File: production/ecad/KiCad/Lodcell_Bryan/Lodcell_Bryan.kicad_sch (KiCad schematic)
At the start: 24 parts, among them J1 LoadCellConnector, J2 power_for_Loadcell, J3 ConnToESP32, U3 ADS1231IDR, U4 TXB0104DR

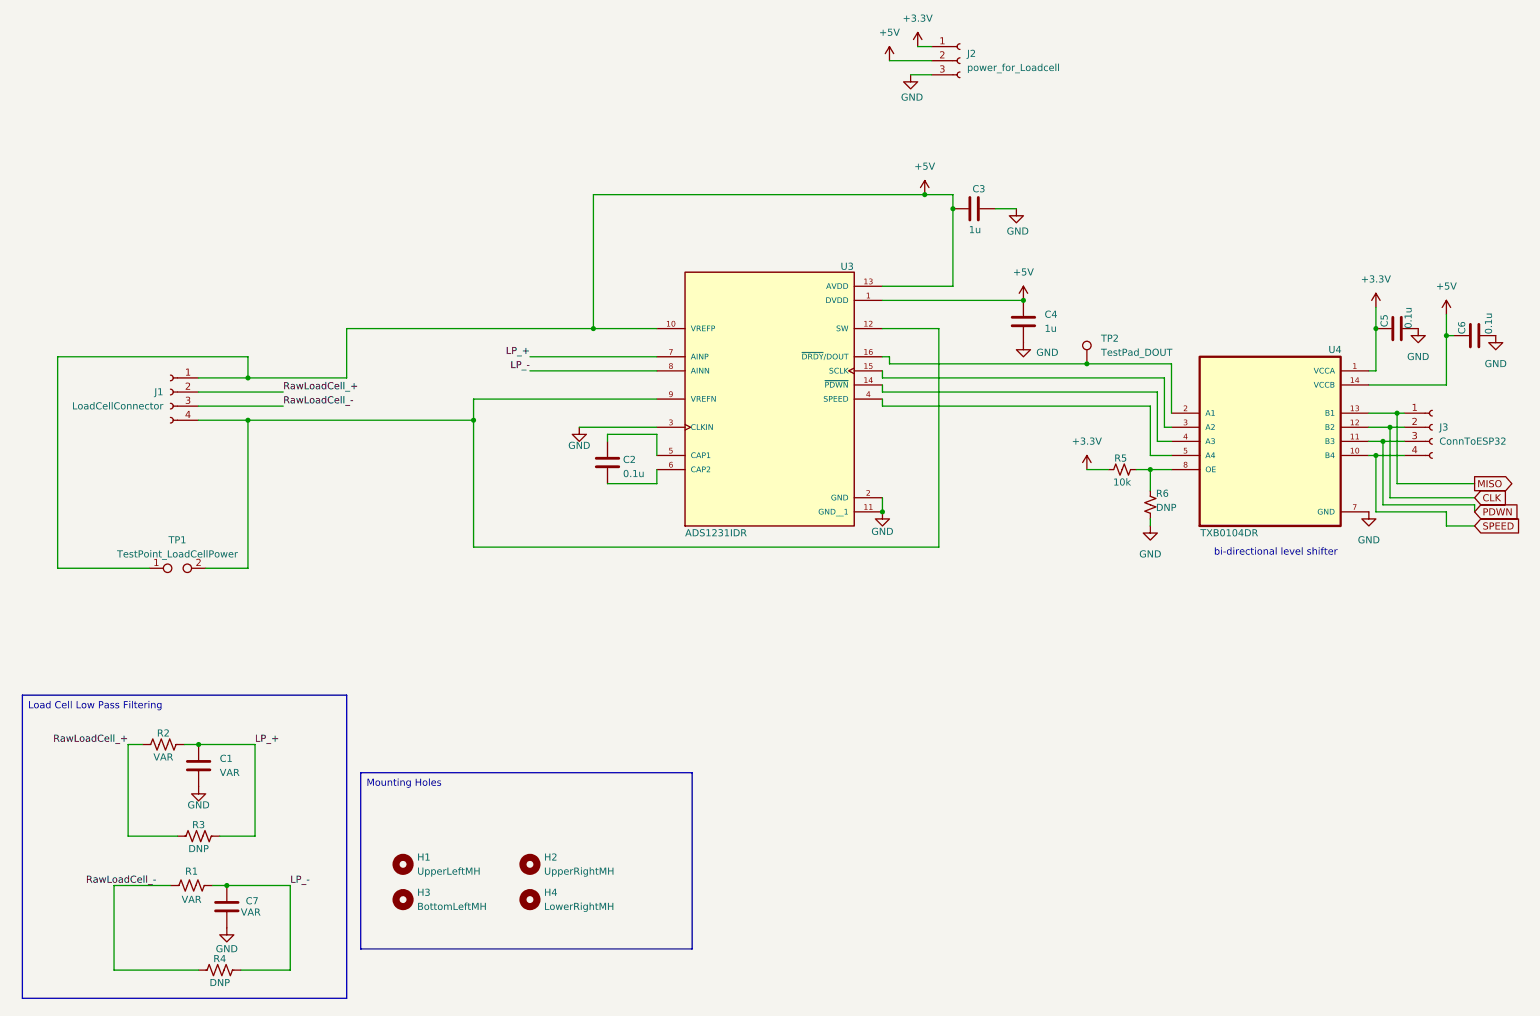
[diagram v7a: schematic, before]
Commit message: Renamed designators
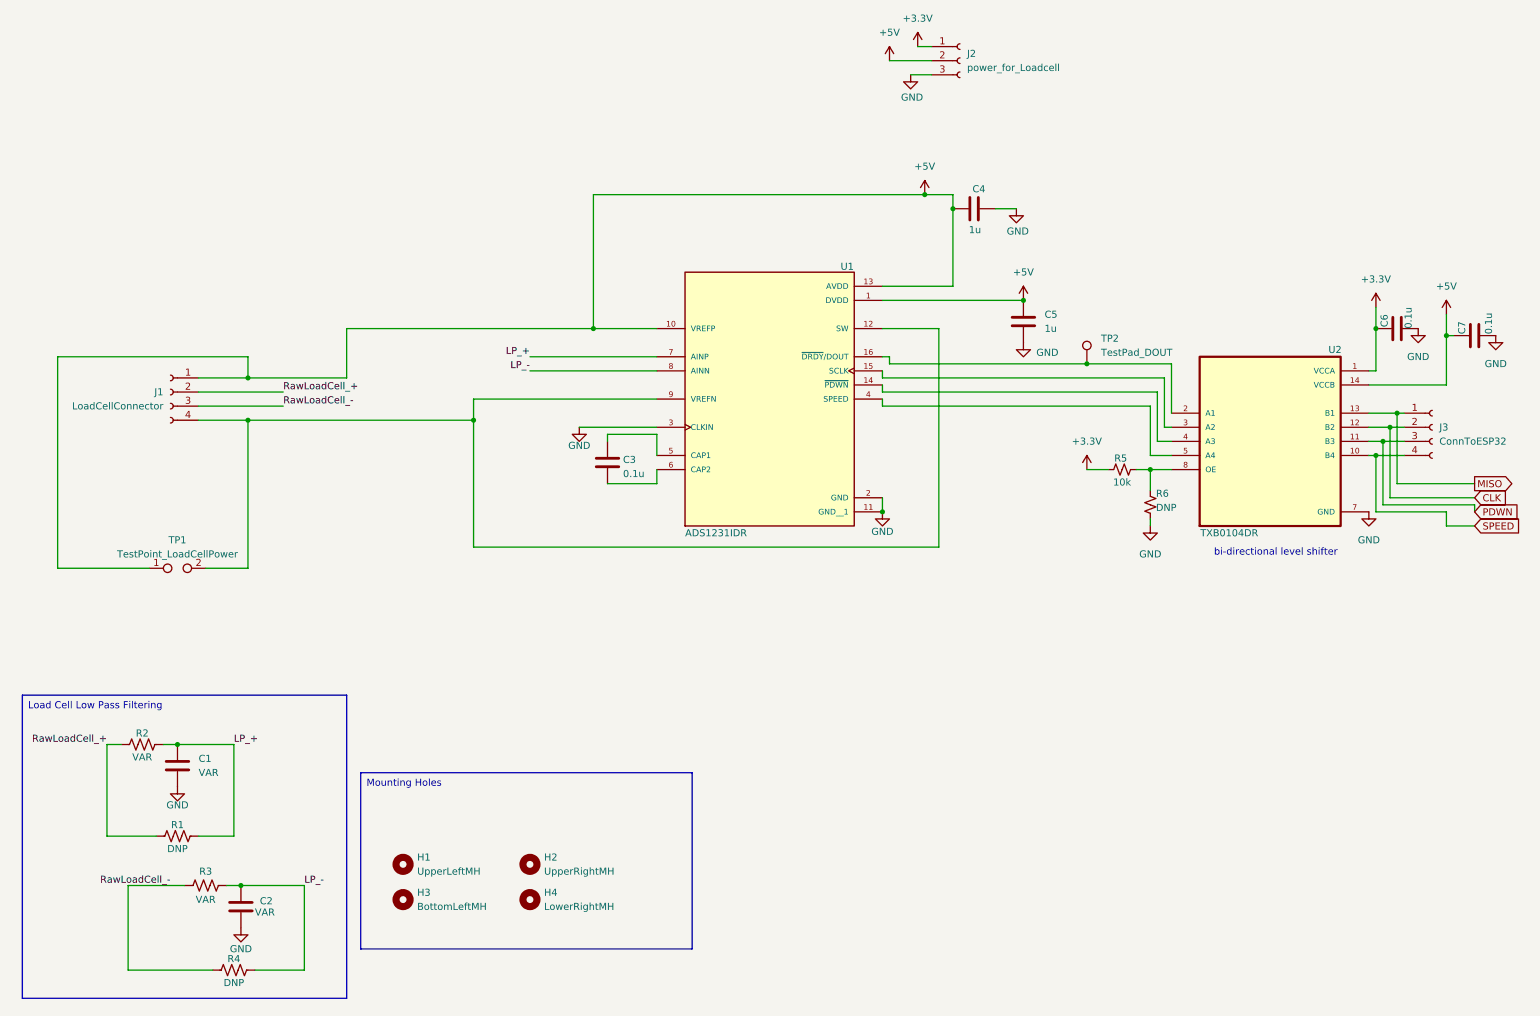
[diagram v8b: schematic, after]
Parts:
- renumbered C7 to C2, C2 to C3, C3 to C4, C4 to C5, C5 to C6, C6 to C7, R3 to R1, R1 to R3, U3 to U1, U4 to U2
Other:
- moved on the sheet: C1, C2, R1, R2, R3, R4
